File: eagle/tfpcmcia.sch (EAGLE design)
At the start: 13 parts, among them IC1 CH32V307, IC2 LM1117MPX-3.3, IC3 APS6404L-3SQR-SN, J2 MSD-11-A

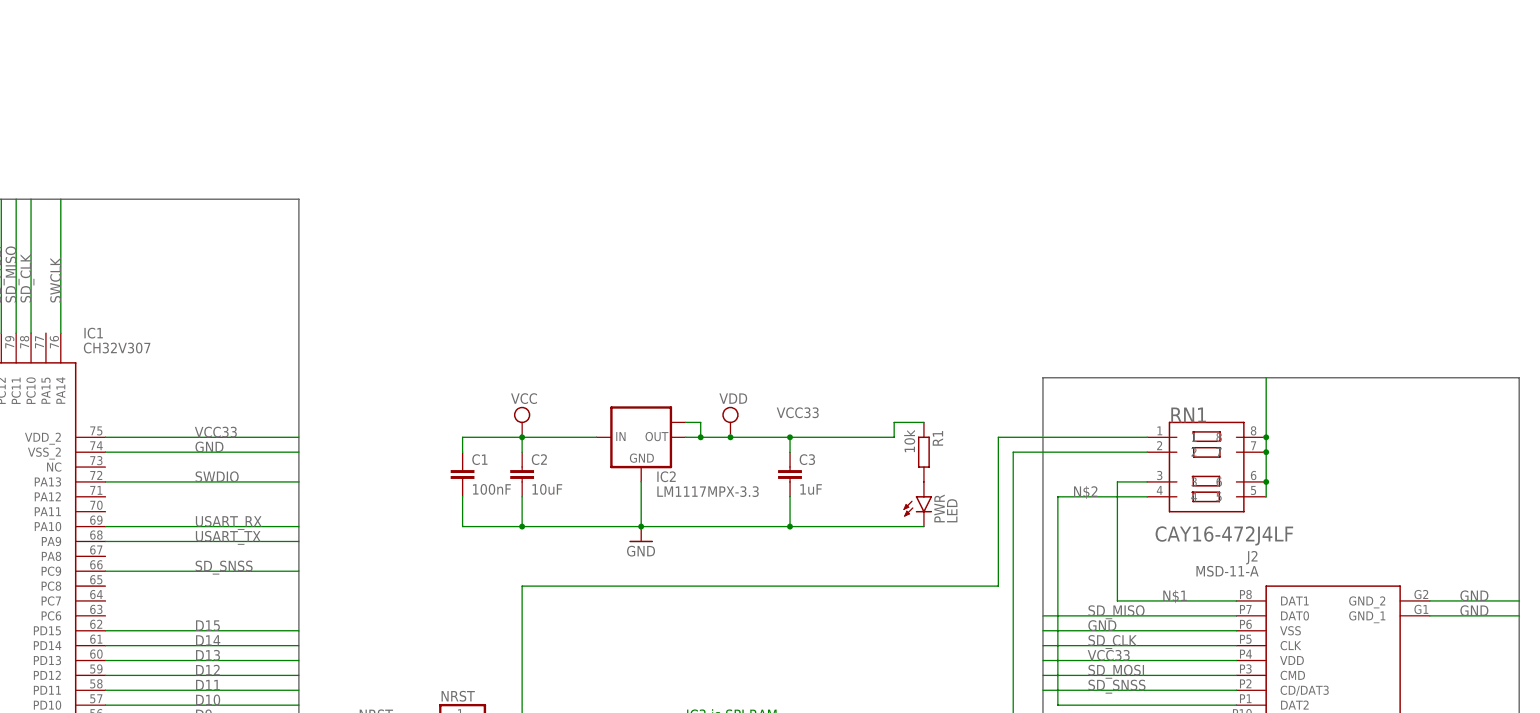
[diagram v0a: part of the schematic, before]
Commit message: Finished routing, unchecked schematic
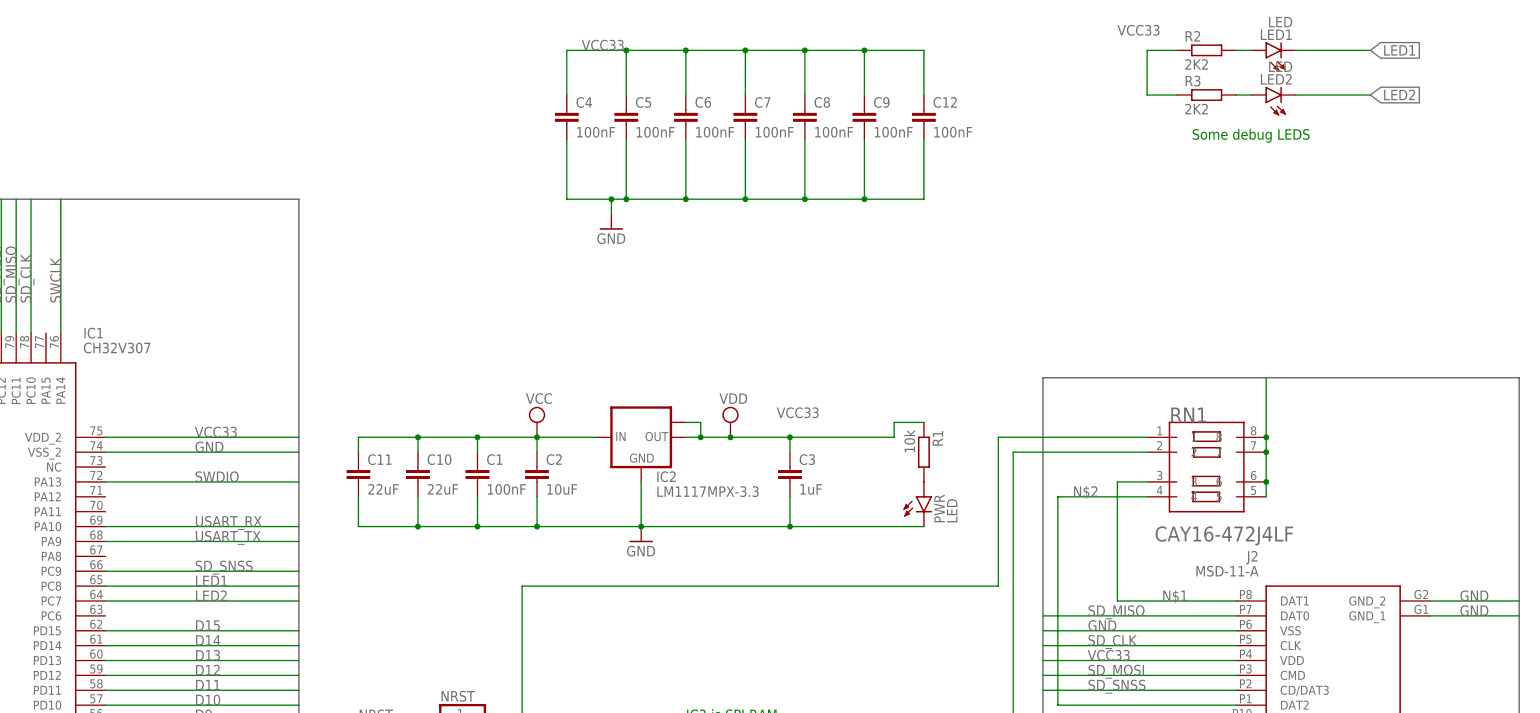
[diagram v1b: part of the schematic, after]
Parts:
- added C10, C11: 22uF, rcl:C-EUC1206
- added C12, C4, C5, C6, C7, C8, C9: 100nF, eagle-ltspice:CC0603
- added LED1, LED2: LED, led:LEDSML0805
- added R2, R3: 2K2, rcl:R-EU_R0603
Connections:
- new net LED1: IC1.PC8, LED1.C
- new net LED2: IC1.PC7, LED2.C
- new net N$5: LED1.A, R2.2
- new net N$6: LED2.A, R3.2
- net GND: now also C10.2, C11.2, C12.2, C4.2, C5.2, C6.2, C7.2, C8.2, C9.2
- net VCC: now also C10.1, C11.1
- net VCC33: now also C12.1, C4.1, C5.1, C6.1, C7.1, C8.1, C9.1, R2.1, R3.1
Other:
- note added: "Some debug LEDS"
- moved on the sheet: C1, C2

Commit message: updated the audio section
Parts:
- added C13, C14: 4.7uF, eagle-ltspice:CC0603
- added C15, C16: 1nF, eagle-ltspice:CC0603
- added C17: 1uF, eagle-ltspice:CC0603
- added C18: 100nF, eagle-ltspice:CC0603
- added IC4: MCP6001RT-I_OT, SamacSys_Parts:MCP6001RT-I_OT
- added R4, R5, R6: 10k, rcl:R-EU_R0603
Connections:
- removed net BVD2: PCMCIA.62
- removed net CD: J2.CD
- new net AUD_MIXED: C14.1, IC1.PA4
- new net AUD_O: C13.1, PCMCIA.62
- new net N$10: C15.1, IC4.VIN-, R4.2, R6.1
- new net N$7: C13.2, C15.2, IC4.VOUT, R6.2
- new net N$8: C16.1, IC4.VIN+, R5.1
- new net N$9: C14.2, R5.2
- new net SD_CD: IC1.PA15, J2.CD
- net GND: now also C16.2, C17.2, C18.2, IC4.VSS, R4.1
- net IORD: now also IC1.PB11
- net IOWR: now also IC1.PB12
- net VCC: now also C17.1, C18.1, IC4.VDD
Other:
- moved on the sheet: C12, C4, C5, C6, C7, C8, C9, LED1, LED2, R2, R3

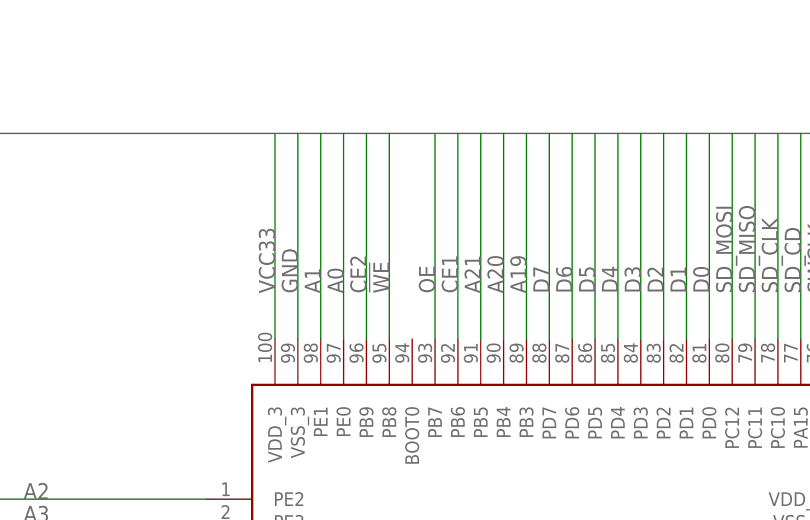
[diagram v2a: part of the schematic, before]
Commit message: fixed BOOT0
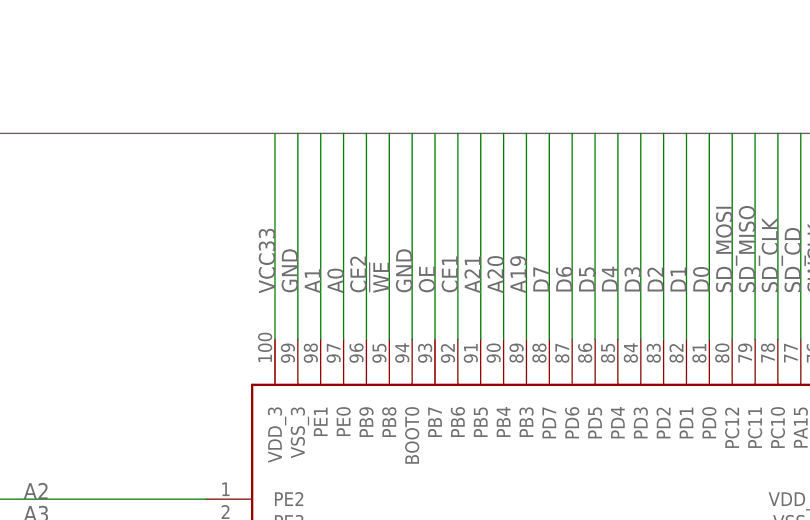
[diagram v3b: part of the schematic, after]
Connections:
- net GND: now also IC1.BOOT0
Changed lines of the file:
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@@
 <label x="383.54" y="-2.54" size="1.778" layer="95"/>
+</segment>
+<segment>
+<pinref part="IC1" gate="G$1" pin="BOOT0"/>
+<wire x1="119.38" y1="119.38" x2="119.38" y2="142.24" width="0.1524" layer="91"/>
+<label x="119.38" y="124.46" size="1.778" layer="95" rot="R90"/>
 </segment>
 </net>

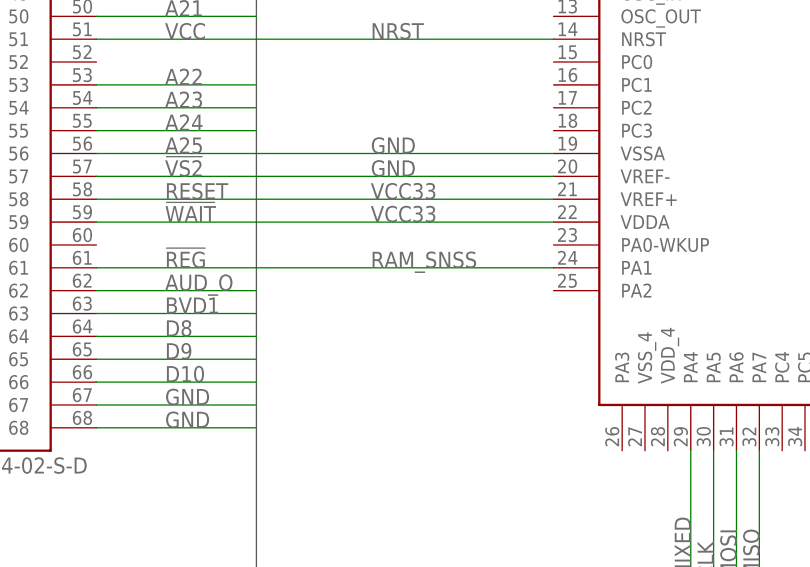
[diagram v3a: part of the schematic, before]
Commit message: Updated READY signal and updated pinout specs
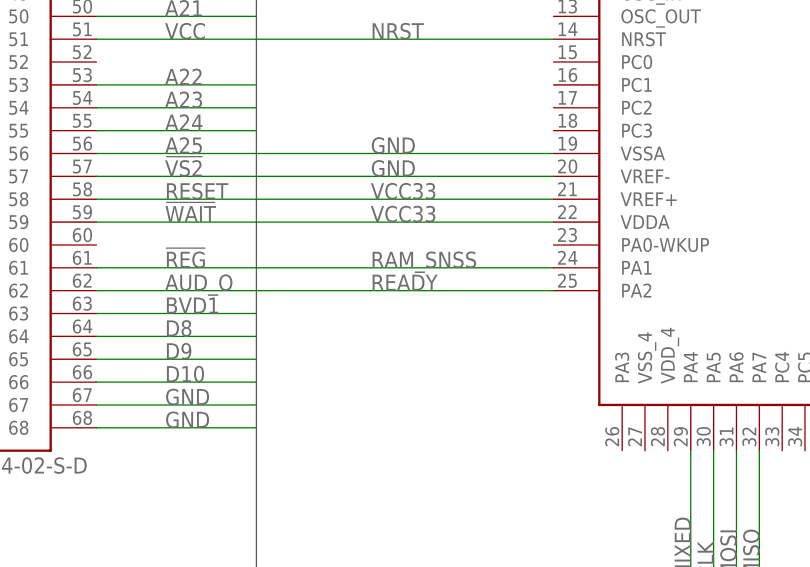
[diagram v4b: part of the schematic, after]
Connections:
- net READY: now also IC1.PA2
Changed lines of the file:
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@@
 <label x="7.62" y="71.12" size="1.778" layer="95"/>
+</segment>
+<segment>
+<pinref part="IC1" gate="G$1" pin="PA2"/>
+<wire x1="96.52" y1="40.64" x2="63.5" y2="40.64" width="0.1524" layer="91"/>
+<label x="76.2" y="40.64" size="1.778" layer="95"/>
 </segment>
 </net>

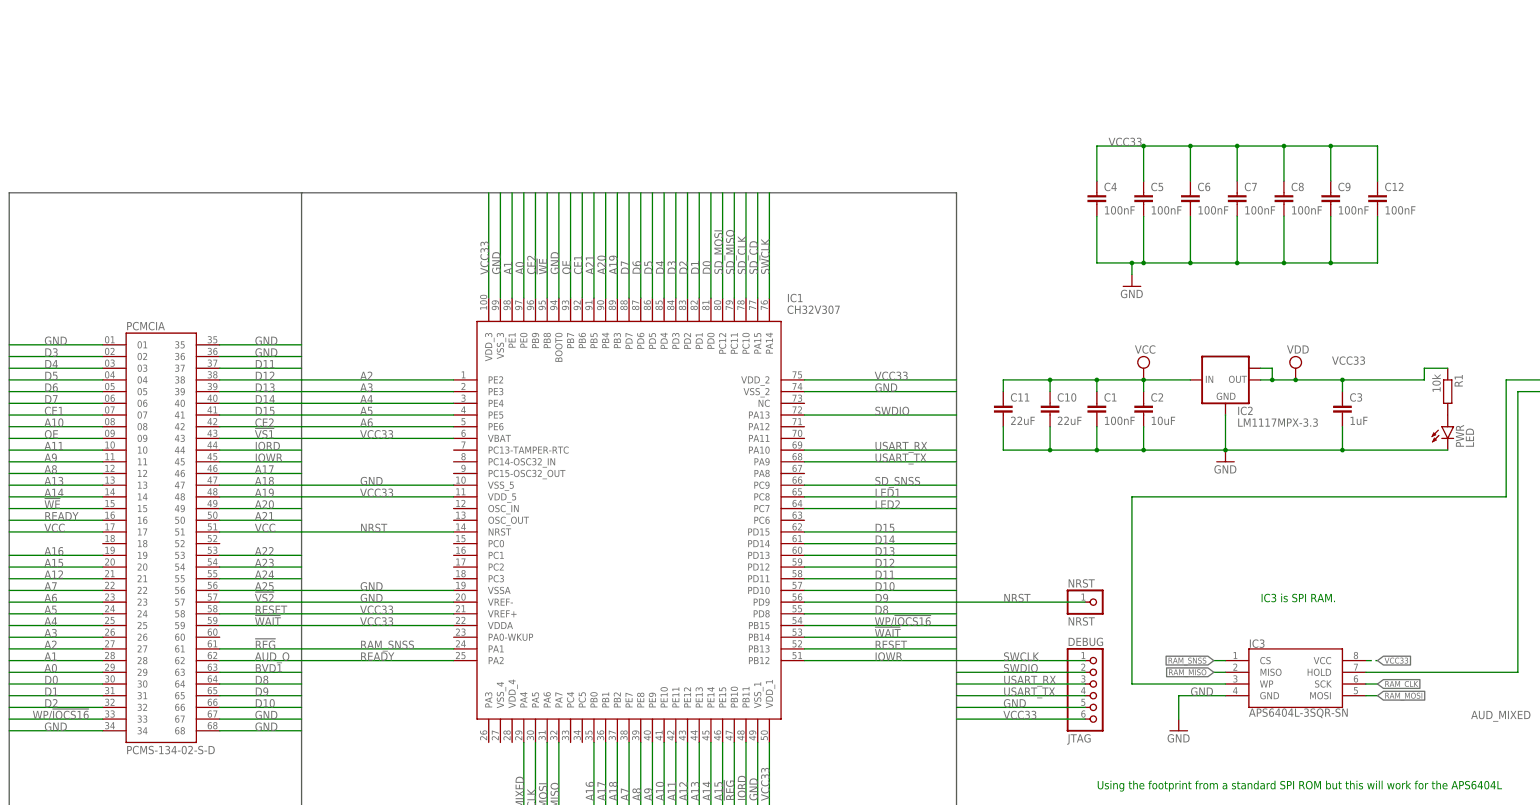
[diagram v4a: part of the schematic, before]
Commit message: added blinkenlights and gathered notes on spi ram usage
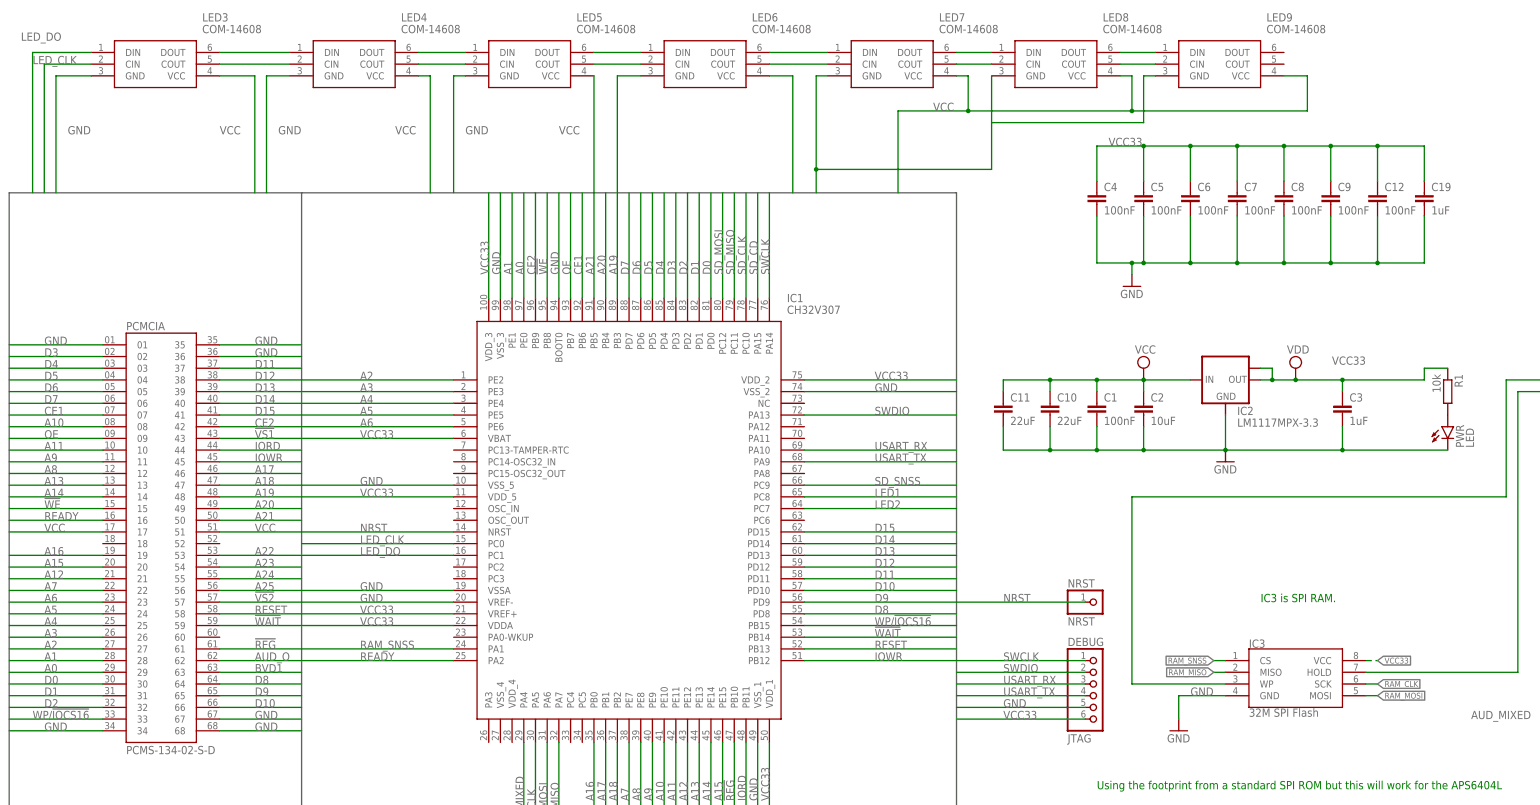
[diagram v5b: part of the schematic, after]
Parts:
- added C19: 1uF, eagle-ltspice:CC0603
- added LED3, LED4, LED5, LED6, LED7, LED8, LED9: COM-14608, Blinkenlights:COM-14608
- IC3: value APS6404L-3SQR-SN -> 32M SPI Flash
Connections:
- new net LED_CLK: IC1.PC0, LED3.CIN
- new net LED_DO: IC1.PC1, LED3.DIN
- new net N$11: LED4.COUT, LED5.CIN
- new net N$12: LED4.DOUT, LED5.DIN
- new net N$13: LED5.DOUT, LED6.DIN
- new net N$14: LED5.COUT, LED6.CIN
- new net N$15: LED3.COUT, LED4.CIN
- new net N$16: LED3.DOUT, LED4.DIN
- new net N$17: LED6.COUT, LED7.CIN
- new net N$19: LED6.DOUT, LED7.DIN
- new net N$20: LED7.DOUT, LED8.DIN
- new net N$21: LED7.COUT, LED8.CIN
- new net N$22: LED8.COUT, LED9.CIN
- new net N$23: LED8.DOUT, LED9.DIN
- net GND: now also C19.2, LED3.GND, LED4.GND, LED5.GND, LED6.GND, LED7.GND, LED8.GND, LED9.GND
- net VCC: now also LED3.VCC, LED4.VCC, LED5.VCC, LED6.VCC, LED7.VCC, LED8.VCC, LED9.VCC
- net VCC33: now also C19.1

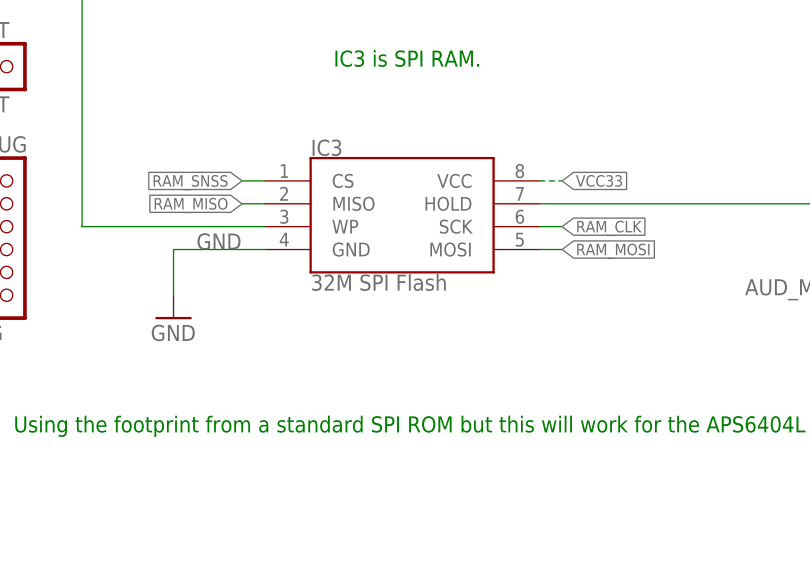
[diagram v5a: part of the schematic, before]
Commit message: add initial firmware: CH32V307 PCMCIA bus emulation returning BEEF/BABE
- Dockerised build using local MRS toolchain (riscv-none-embed-gcc)
- EXTI9_5 VTF interrupt handler drives data bus on UDS/LDS assertion
- Common memory returns 0xBEEF, attribute memory returns 0xBABE
- BUS16() macro compensates for Gayle byte-lane swap on A600/A1200
- UART debug on PA9 at 115200, heartbeat LED on PC8
- Top-level Makefile delegates build/clean to Docker container
- DiagROM helper scripts in scripts/
- Updated .gitignore for firmware build artefacts and MRS installer
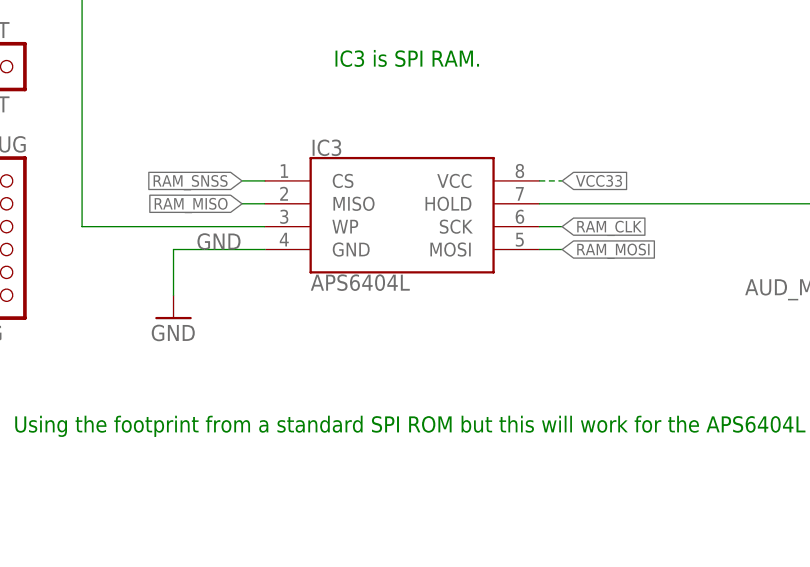
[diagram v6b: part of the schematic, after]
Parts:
- IC3: value 32M SPI Flash -> APS6404L
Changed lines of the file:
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@@
 <part name="J2" library="SamacSys_Parts" deviceset="MSD-11-A" device=""/>
 <part name="RN1" library="CAY16-103J4LF" deviceset="CAY16-103J4LF" device="" value="CAY16-472J4LF"/>
-<part name="IC3" library="SparkFun-IC-Memory" deviceset="SPI_FLASH-X25XX" device="SMD" value="32M SPI Flash"/>
+<part name="IC3" library="SparkFun-IC-Memory" deviceset="SPI_FLASH-X25XX" device="SMD" value="APS6404L"/>
 <part name="GND1" library="supply1" library_urn="urn:adsk.eagle:library:371" deviceset="GND" device=""/>
 <part name="NRST" library="pinhead" library_urn="urn:adsk.eagle:library:325" deviceset="PINHD-1X1" device="" package3d_urn="urn:adsk.eagle:package:22485/2" value="NRST"/>
